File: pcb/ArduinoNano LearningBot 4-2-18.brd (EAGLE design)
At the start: 106.9 x 60.1 mm, 20 parts

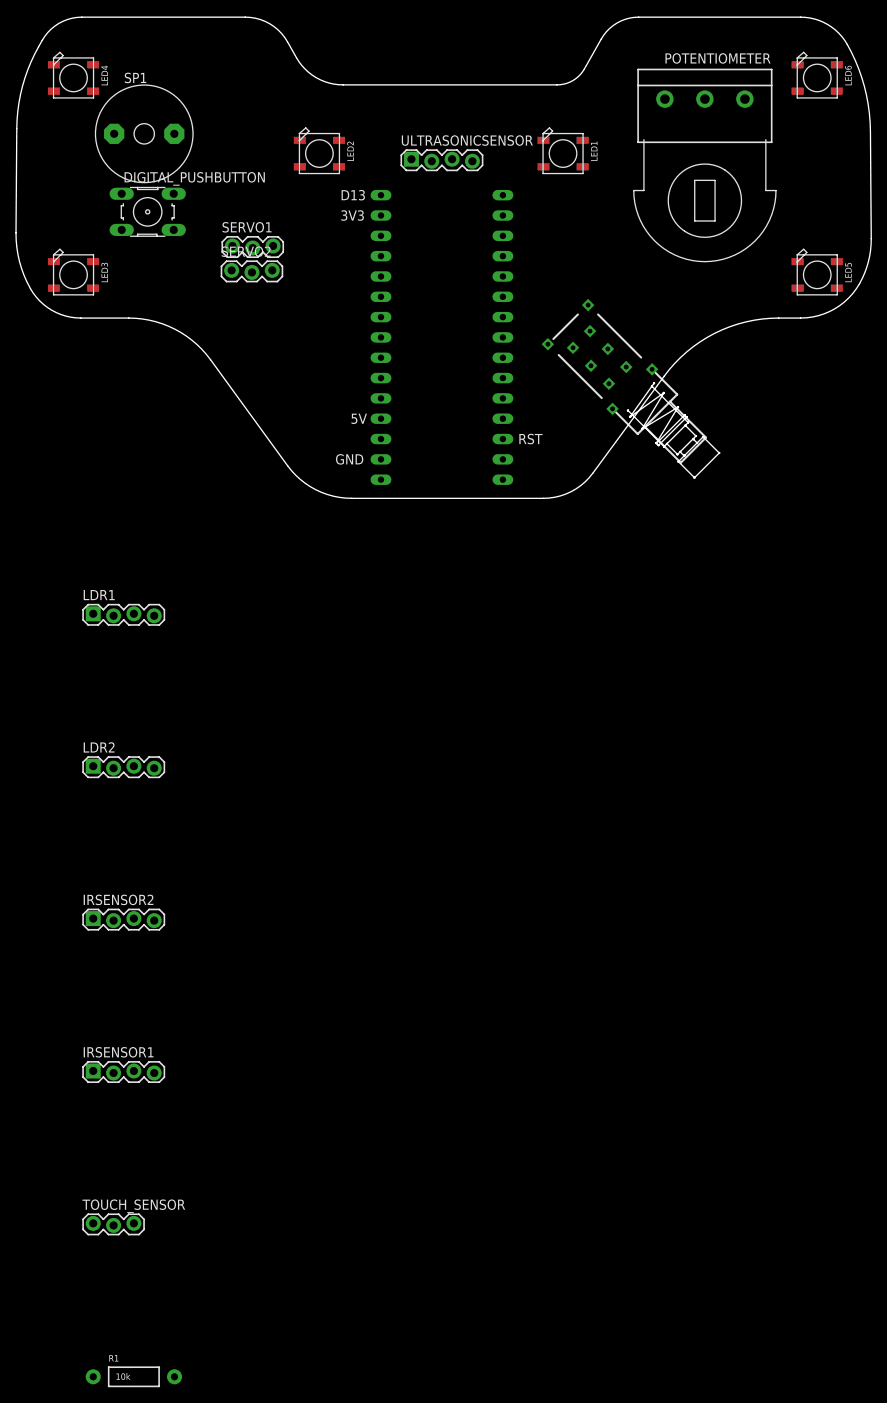
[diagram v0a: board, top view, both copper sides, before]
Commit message: With components placed
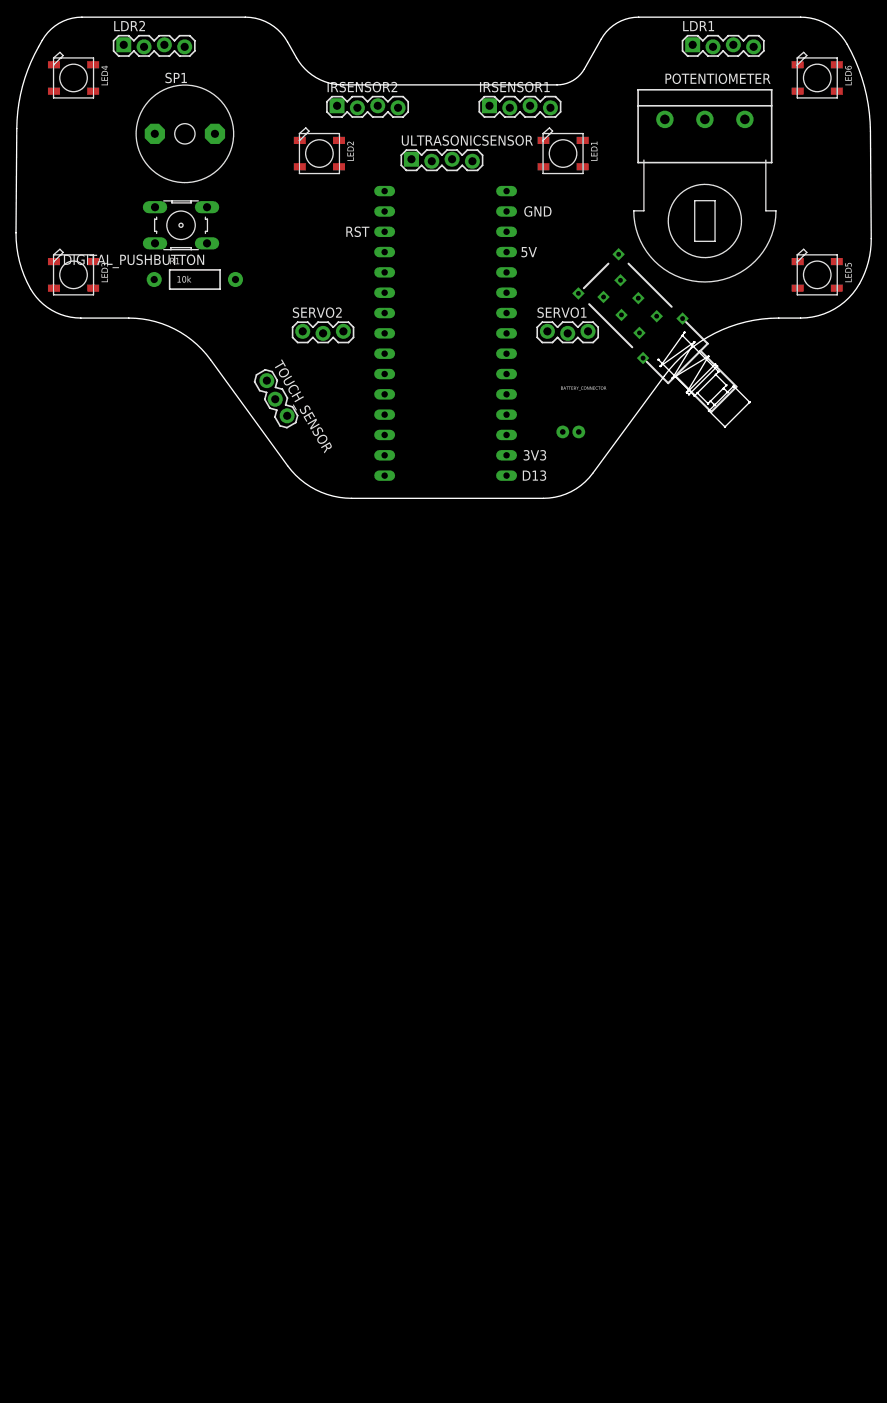
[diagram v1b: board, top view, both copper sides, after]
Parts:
- added BATTERY_CONNECTOR: (no value), SparkFun-Connectors:JST-2-PTH-NS
- moved R1 137.4 mm to (26.7, 31.8)
- moved IRSENSOR1 130.4 mm to (63.5, 53.3)
- moved TOUCH_SENSOR 107.6 mm to (35.6, 19.1), turned to 300 degrees
- moved IRSENSOR2 106.1 mm to (44.5, 53.3)
- moved LDR1 103.3 mm to (88.9, 61.0)
- moved LDR2 90.3 mm to (17.8, 61.0)
- moved SERVO1 40.8 mm to (70.7, 25.1)
- moved U$1 18.9 mm to (55.5, 33.9), turned to 180 degrees
- moved SERVO2 11.7 mm to (40.2, 25.1)
- moved POWER_SWITCH 7.41 mm to (80.9, 28.2)
- moved SP1 5.08 mm to (25.4, 50.0)
- moved DIGITAL_PUSHBUTTON 4.49 mm to (24.9, 38.5), turned to 180 degrees
- moved POTENTIOMETER 2.54 mm to (90.4, 51.8)
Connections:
- new net N$1: LED2.4-DIN, U$1.D10
- new net N$2: LED1.4-DIN, LED2.2-DOUT
- new net N$4: LED1.2-DOUT, LED4.4-DIN
- new net N$5: LED4.2-DOUT, LED6.4-DIN
- new net N$6: LED3.4-DIN, LED6.2-DOUT
- new net N$8: LED3.2-DOUT, LED5.4-DIN
- net GND: now also U$1.GND1
- net IR_SENSOR2_AO: now also POWER_SWITCH.NC1
